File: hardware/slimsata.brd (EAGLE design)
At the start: 20.3 x 54.6 mm, 2 parts, among them CON1 MOLEX_67492, CON2 MOLEX_47300

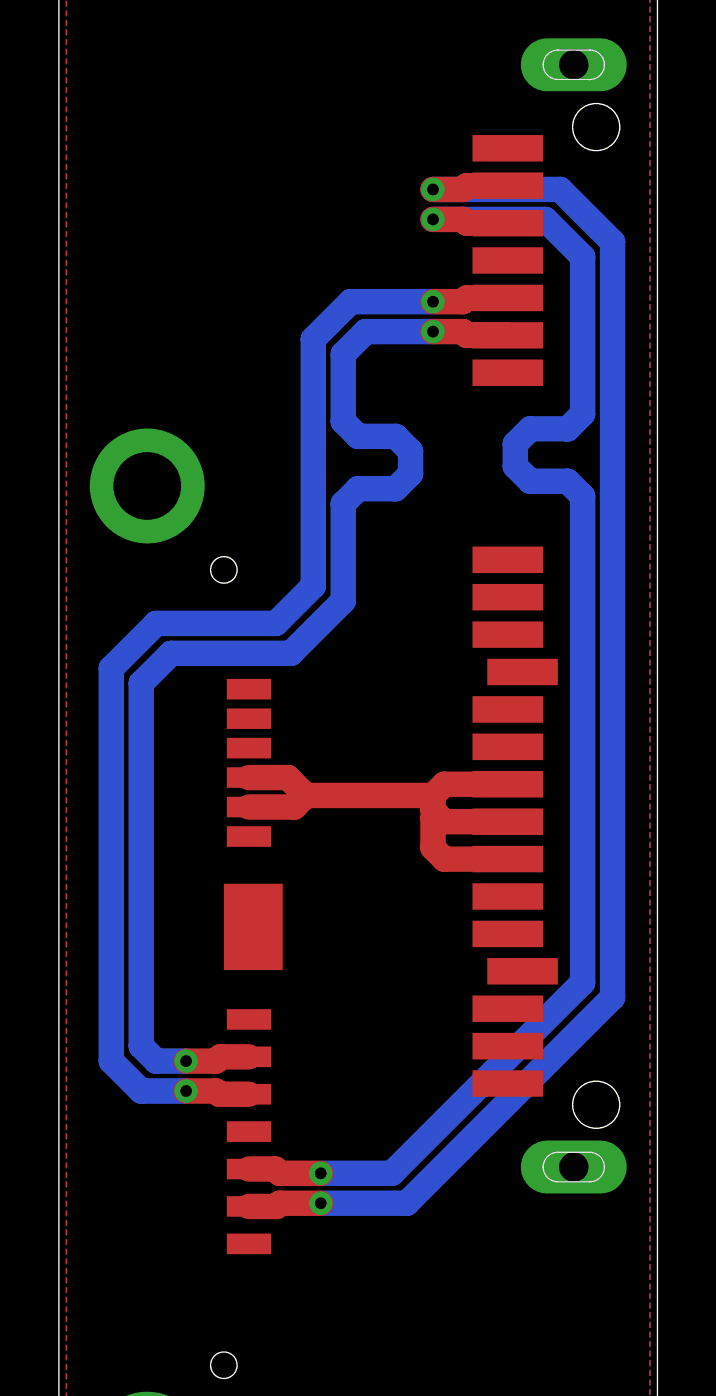
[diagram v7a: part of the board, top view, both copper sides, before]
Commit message: andere Leitungsführung der Datenleitungen, ohne Längenausgleich
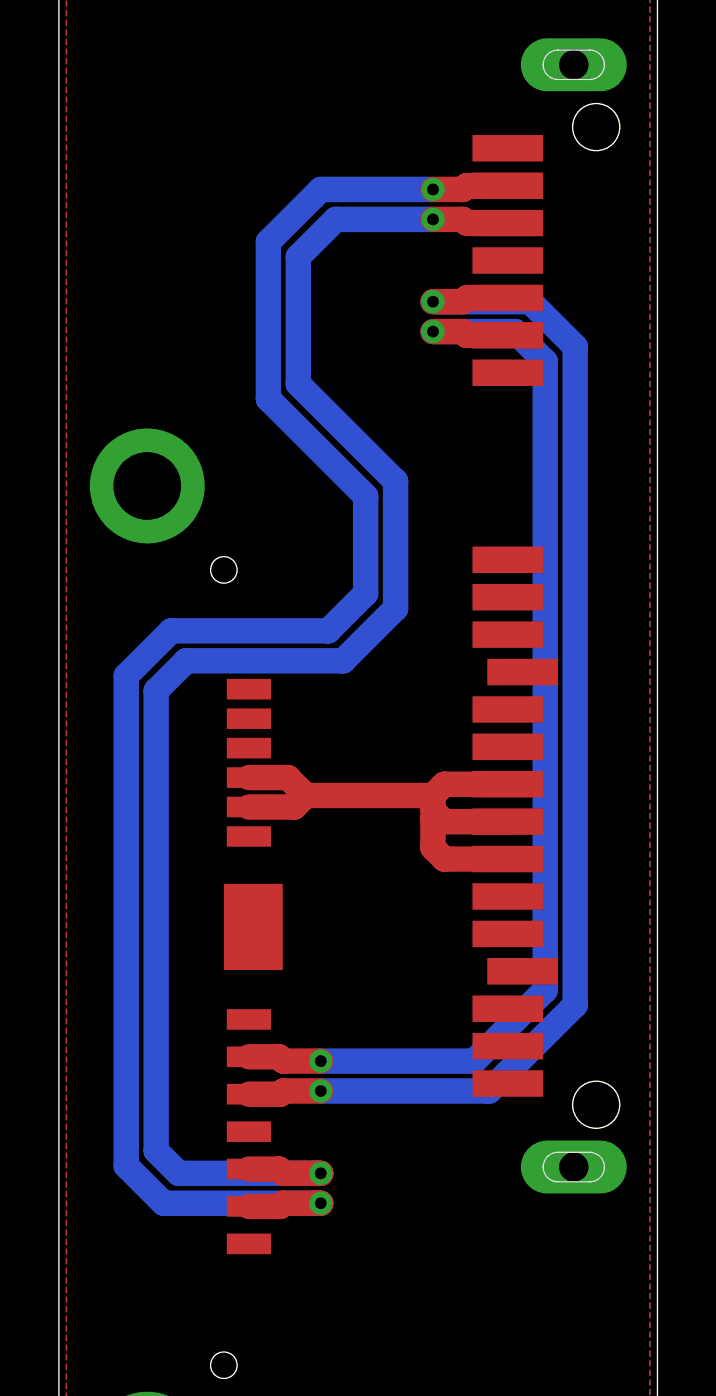
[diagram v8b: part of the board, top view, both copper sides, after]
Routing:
- net N$5: track 50.4 -> 58.0 mm
- net N$6: track 50.3 -> 54.6 mm
- net N$8: track 42.0 -> 39.3 mm
- net N$7: track 42.1 -> 42.7 mm
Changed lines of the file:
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@@
 <wire x1="13.716" y1="47.498" x2="12.7" y2="47.498" width="0.8636" layer="1"/>
 <via x="12.7" y="47.498" extent="1-16" drill="0.4"/>
-<wire x1="12.7" y1="47.498" x2="17.018" y2="47.498" width="0.8636" layer="16"/>
-<wire x1="17.018" y1="47.498" x2="18.796" y2="45.72" width="0.8636" layer="16"/>
-<wire x1="18.796" y1="20.066" x2="18.796" y2="45.72" width="0.8636" layer="16"/>
-<wire x1="18.796" y1="20.066" x2="11.811" y2="13.081" width="0.8636" layer="16"/>
-<wire x1="11.811" y1="13.081" x2="8.89" y2="13.081" width="0.8636" layer="16"/>
+<wire x1="12.7" y1="47.498" x2="8.89" y2="47.498" width="0.8636" layer="16"/>
+<wire x1="8.89" y1="47.498" x2="7.112" y2="45.72" width="0.8636" layer="16"/>
+<wire x1="7.112" y1="45.72" x2="7.112" y2="40.386" width="0.8636" layer="16"/>
+<wire x1="7.112" y1="40.386" x2="10.414" y2="37.084" width="0.8636" layer="16"/>
+<wire x1="10.414" y1="37.084" x2="10.414" y2="33.782" width="0.8636" layer="16"/>
+<wire x1="10.414" y1="33.782" x2="9.144" y2="32.512" width="0.8636" layer="16"/>
+<wire x1="9.144" y1="32.512" x2="3.81" y2="32.512" width="0.8636" layer="16"/>
+<wire x1="3.81" y1="32.512" x2="2.286" y2="30.988" width="0.8636" layer="16"/>
+<wire x1="2.286" y1="30.988" x2="2.286" y2="14.351" width="0.8636" layer="16"/>
+<wire x1="2.286" y1="14.351" x2="3.556" y2="13.081" width="0.8636" layer="16"/>
+<wire x1="3.556" y1="13.081" x2="8.89" y2="13.081" width="0.8636" layer="16"/>
 <via x="8.89" y="13.081" extent="1-16" drill="0.4"/>
-<wire x1="6.45" y1="12.972" x2="7.384" y2="12.972" width="0.8636" layer="1"/>
-<wire x1="7.384" y1="12.972" x2="7.493" y2="13.081" width="0.8636" layer="1"/>
-<wire x1="7.493" y1="13.081" x2="8.89" y2="13.081" width="0.8636" layer="1"/>
+<wire x1="8.89" y1="13.081" x2="8.636" y2="13.081" width="0.8636" layer="1"/>
+<wire x1="6.45" y1="12.972" x2="7.511" y2="12.972" width="0.8636" layer="1"/>
+<wire x1="7.511" y1="12.972" x2="7.62" y2="13.081" width="0.8636" layer="1"/>
+<wire x1="7.62" y1="13.081" x2="8.89" y2="13.081" width="0.8636" layer="1"/>
 </signal>
 <signal name="N$6" class="1">
@@
 <wire x1="13.716" y1="46.482" x2="12.7" y2="46.482" width="0.8636" layer="1"/>
 <via x="12.7" y="46.482" extent="1-16" drill="0.4"/>
-<wire x1="12.7" y1="46.482" x2="16.51" y2="46.482" width="0.8636" layer="16"/>
-<wire x1="16.51" y1="46.482" x2="17.78" y2="45.212" width="0.8636" layer="16"/>
-<wire x1="17.78" y1="45.212" x2="17.78" y2="39.878" width="0.8636" layer="16"/>
-<wire x1="17.78" y1="39.878" x2="17.272" y2="39.37" width="0.8636" layer="16"/>
-<wire x1="17.272" y1="39.37" x2="16.002" y2="39.37" width="0.8636" layer="16"/>
-<wire x1="16.002" y1="39.37" x2="15.494" y2="38.862" width="0.8636" layer="16"/>
-<wire x1="15.494" y1="38.862" x2="15.494" y2="38.1" width="0.8636" layer="16"/>
-<wire x1="15.494" y1="38.1" x2="16.002" y2="37.592" width="0.8636" layer="16"/>
-<wire x1="16.002" y1="37.592" x2="17.272" y2="37.592" width="0.8636" layer="16"/>
-<wire x1="17.272" y1="37.592" x2="17.78" y2="37.084" width="0.8636" layer="16"/>
-<wire x1="17.78" y1="37.084" x2="17.78" y2="20.574" width="0.8636" layer="16"/>
-<wire x1="17.78" y1="20.574" x2="11.303" y2="14.097" width="0.8636" layer="16"/>
-<wire x1="11.303" y1="14.097" x2="8.89" y2="14.097" width="0.8636" layer="16"/>
+<wire x1="12.7" y1="46.482" x2="9.398" y2="46.482" width="0.8636" layer="16"/>
+<wire x1="9.398" y1="46.482" x2="8.128" y2="45.212" width="0.8636" layer="16"/>
+<wire x1="8.128" y1="45.212" x2="8.128" y2="40.894" width="0.8636" layer="16"/>
+<wire x1="8.128" y1="40.894" x2="11.43" y2="37.592" width="0.8636" layer="16"/>
+<wire x1="11.43" y1="37.592" x2="11.43" y2="33.274" width="0.8636" layer="16"/>
+<wire x1="11.43" y1="33.274" x2="9.652" y2="31.496" width="0.8636" layer="16"/>
+<wire x1="9.652" y1="31.496" x2="4.318" y2="31.496" width="0.8636" layer="16"/>
+<wire x1="4.318" y1="31.496" x2="3.302" y2="30.48" width="0.8636" layer="16"/>
+<wire x1="3.302" y1="30.48" x2="3.302" y2="14.859" width="0.8636" layer="16"/>
+<wire x1="3.302" y1="14.859" x2="4.064" y2="14.097" width="0.8636" layer="16"/>
+<wire x1="4.064" y1="14.097" x2="8.89" y2="14.097" width="0.8636" layer="16"/>
 <via x="8.89" y="14.097" extent="1-16" drill="0.4"/>
-<wire x1="6.45" y1="14.242" x2="7.348" y2="14.242" width="0.8636" layer="1"/>
-<wire x1="7.348" y1="14.242" x2="7.493" y2="14.097" width="0.8636" layer="1"/>
-<wire x1="7.493" y1="14.097" x2="8.89" y2="14.097" width="0.8636" layer="1"/>
+<wire x1="8.89" y1="14.097" x2="8.636" y2="14.097" width="0.8636" layer="1"/>
+<wire x1="6.45" y1="14.242" x2="7.475" y2="14.242" width="0.8636" layer="1"/>
+<wire x1="7.475" y1="14.242" x2="7.62" y2="14.097" width="0.8636" layer="1"/>
+<wire x1="7.62" y1="14.097" x2="8.89" y2="14.097" width="0.8636" layer="1"/>
 </signal>
 <signal name="N$7" class="1">
@@
 <wire x1="13.716" y1="43.688" x2="12.7" y2="43.688" width="0.8636" layer="1"/>
 <via x="12.7" y="43.688" extent="1-16" drill="0.4"/>
-<wire x1="12.7" y1="43.688" x2="9.906" y2="43.688" width="0.8636" layer="16"/>
-<wire x1="9.906" y1="43.688" x2="8.636" y2="42.418" width="0.8636" layer="16"/>
-<wire x1="8.636" y1="34.036" x2="8.636" y2="42.418" width="0.8636" layer="16"/>
-<wire x1="8.636" y1="34.036" x2="7.366" y2="32.766" width="0.8636" layer="16"/>
-<wire x1="7.366" y1="32.766" x2="3.302" y2="32.766" width="0.8636" layer="16"/>
-<wire x1="3.302" y1="32.766" x2="1.778" y2="31.242" width="0.8636" layer="16"/>
-<wire x1="1.778" y1="31.242" x2="1.778" y2="17.907" width="0.8636" layer="16"/>
-<wire x1="1.778" y1="17.907" x2="2.794" y2="16.891" width="0.8636" layer="16"/>
-<wire x1="2.794" y1="16.891" x2="4.318" y2="16.891" width="0.8636" layer="16"/>
-<via x="4.318" y="16.891" extent="1-16" drill="0.4"/>
-<wire x1="6.45" y1="16.782" x2="5.443" y2="16.782" width="0.8636" layer="1"/>
-<wire x1="5.443" y1="16.782" x2="5.334" y2="16.891" width="0.8636" layer="1"/>
-<wire x1="5.334" y1="16.891" x2="4.318" y2="16.891" width="0.8636" layer="1"/>
+<wire x1="12.7" y1="43.688" x2="16.002" y2="43.688" width="0.8636" layer="16"/>
+<wire x1="16.002" y1="43.688" x2="17.526" y2="42.164" width="0.8636" layer="16"/>
+<wire x1="17.526" y1="42.164" x2="17.526" y2="19.812" width="0.8636" layer="16"/>
+<wire x1="17.526" y1="19.812" x2="14.605" y2="16.891" width="0.8636" layer="16"/>
+<wire x1="14.605" y1="16.891" x2="8.89" y2="16.891" width="0.8636" layer="16"/>
+<wire x1="6.45" y1="16.782" x2="7.511" y2="16.782" width="0.8636" layer="1"/>
+<wire x1="7.511" y1="16.782" x2="7.62" y2="16.891" width="0.8636" layer="1"/>
+<wire x1="7.62" y1="16.891" x2="8.89" y2="16.891" width="0.8636" layer="1"/>
+<via x="8.89" y="16.891" extent="1-16" drill="0.4"/>
 </signal>
 <signal name="N$8" class="1">
@@
 <wire x1="13.716" y1="42.672" x2="12.7" y2="42.672" width="0.8636" layer="1"/>
 <via x="12.7" y="42.672" extent="1-16" drill="0.4"/>
-<wire x1="12.7" y1="42.672" x2="10.414" y2="42.672" width="0.8636" layer="16"/>
-<wire x1="10.414" y1="42.672" x2="9.652" y2="41.91" width="0.8636" layer="16"/>
-<wire x1="9.652" y1="41.91" x2="9.652" y2="39.624" width="0.8636" layer="16"/>
-<wire x1="9.652" y1="39.624" x2="10.16" y2="39.116" width="0.8636" layer="16"/>
-<wire x1="10.16" y1="39.116" x2="11.43" y2="39.116" width="0.8636" layer="16"/>
-<wire x1="11.43" y1="39.116" x2="11.938" y2="38.608" width="0.8636" layer="16"/>
-<wire x1="11.938" y1="37.846" x2="11.938" y2="38.608" width="0.8636" layer="16"/>
-<wire x1="11.938" y1="37.846" x2="11.43" y2="37.338" width="0.8636" layer="16"/>
-<wire x1="11.43" y1="37.338" x2="10.16" y2="37.338" width="0.8636" layer="16"/>
-<wire x1="10.16" y1="37.338" x2="9.652" y2="36.83" width="0.8636" layer="16"/>
-<wire x1="9.652" y1="36.83" x2="9.652" y2="33.528" width="0.8636" layer="16"/>
-<wire x1="9.652" y1="33.528" x2="7.874" y2="31.75" width="0.8636" layer="16"/>
-<wire x1="7.874" y1="31.75" x2="3.81" y2="31.75" width="0.8636" layer="16"/>
-<wire x1="3.81" y1="31.75" x2="2.794" y2="30.734" width="0.8636" layer="16"/>
-<wire x1="2.794" y1="30.734" x2="2.794" y2="18.415" width="0.8636" layer="16"/>
-<wire x1="3.302" y1="17.907" x2="2.794" y2="18.415" width="0.8636" layer="16"/>
-<wire x1="3.302" y1="17.907" x2="4.318" y2="17.907" width="0.8636" layer="16"/>
-<via x="4.318" y="17.907" extent="1-16" drill="0.4"/>
-<wire x1="6.45" y1="18.052" x2="5.479" y2="18.052" width="0.8636" layer="1"/>
-<wire x1="5.479" y1="18.052" x2="5.334" y2="17.907" width="0.8636" layer="1"/>
-<wire x1="5.334" y1="17.907" x2="4.318" y2="17.907" width="0.8636" layer="1"/>
+<wire x1="12.7" y1="42.672" x2="15.494" y2="42.672" width="0.8636" layer="16"/>
+<wire x1="15.494" y1="42.672" x2="16.51" y2="41.656" width="0.8636" layer="16"/>
+<wire x1="16.51" y1="41.656" x2="16.51" y2="20.32" width="0.8636" layer="16"/>
+<wire x1="16.51" y1="20.32" x2="14.097" y2="17.907" width="0.8636" layer="16"/>
+<wire x1="14.097" y1="17.907" x2="8.89" y2="17.907" width="0.8636" layer="16"/>
+<wire x1="6.45" y1="18.052" x2="7.475" y2="18.052" width="0.8636" layer="1"/>
+<wire x1="7.475" y1="18.052" x2="7.62" y2="17.907" width="0.8636" layer="1"/>
+<wire x1="7.62" y1="17.907" x2="8.89" y2="17.907" width="0.8636" layer="1"/>
+<via x="8.89" y="17.907" extent="1-16" drill="0.4"/>
 </signal>
 <signal name="N$3">
